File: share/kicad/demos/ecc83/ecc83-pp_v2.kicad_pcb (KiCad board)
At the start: 2 copper layers, 48.3 x 41.9 mm, 15 parts, among them P1 IN, P2 OUT, P3 POWER, P4 CONN_2, P5 CONN_1, P6 CONN_1, P7 CONN_1, P8 CONN_1, U1 ECC83

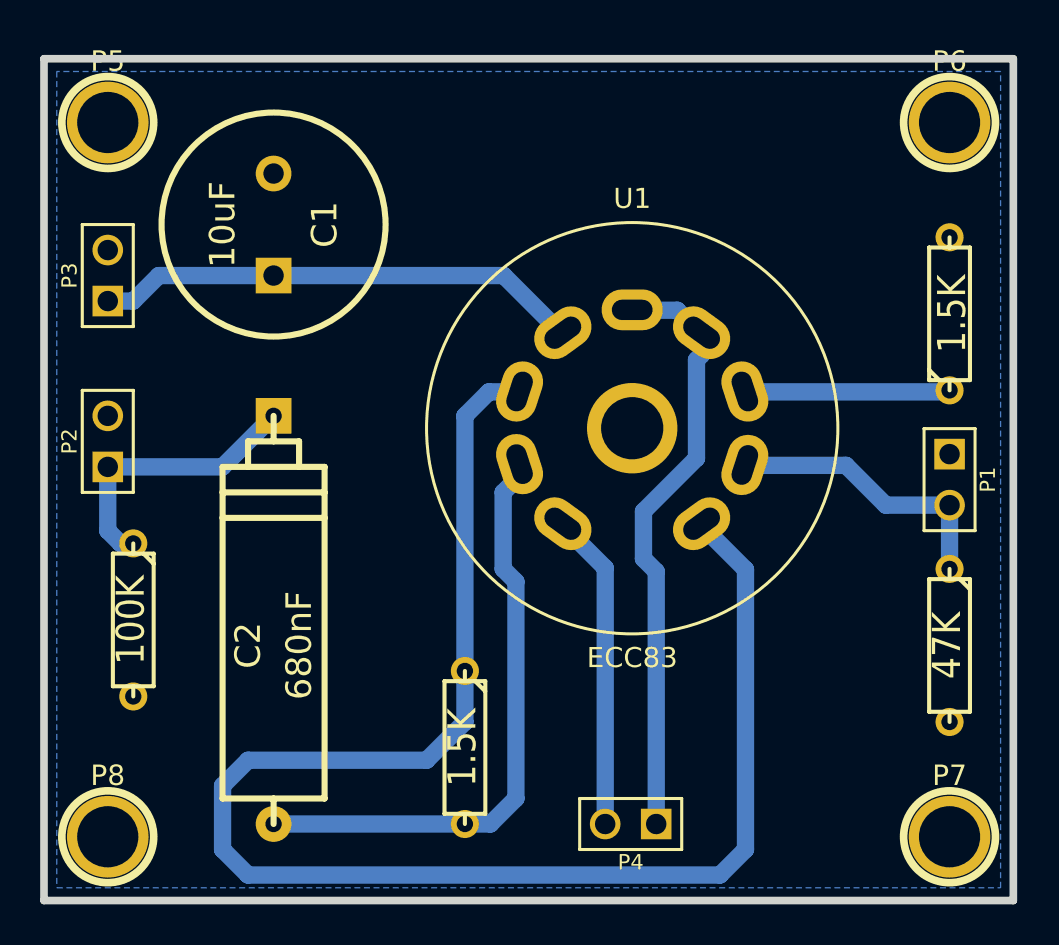
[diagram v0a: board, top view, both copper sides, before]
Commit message: Remove KiCad V4.0.7
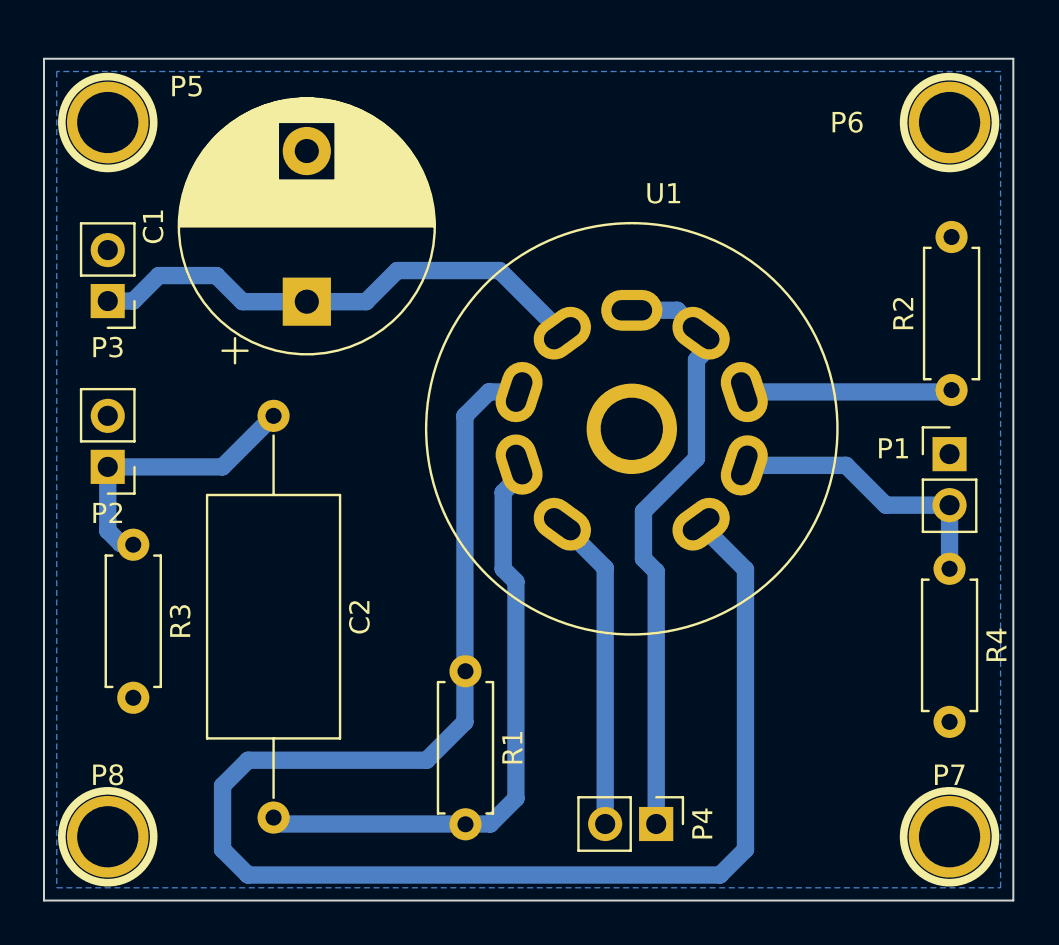
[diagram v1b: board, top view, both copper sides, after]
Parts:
- C1: footprint discret:C2V10 -> Capacitor_THT:CP_Radial_D12.5mm_P7.50mm
- C2: footprint discret:CP8 -> Capacitors_THT:C_Axial_L12.0mm_D6.5mm_P20.00mm_Horizontal
- P1, P2, P3, P4: footprint pin_array:pin_array_1x02 -> Connector_PinHeader_2.54mm:PinHeader_1x02_P2.54mm_Vertical
- R1, R2, R3, R4: footprint discret:R3 -> Resistor_THT:R_Axial_DIN0207_L6.3mm_D2.5mm_P7.62mm_Horizontal
- U1: footprint Valves:VALVE-ECC-83-2 -> Valve:Valve_ECC-83-2
- moved C2 10.2 mm to (131.4, 108.6)
- moved C1 4.18 mm to (133.1, 102.9)
- moved R4 3.81 mm to (165.1, 116.2)
- moved R2 3.80 mm to (165.2, 107.3)
- moved R1 3.80 mm to (141.0, 121.3)
- moved R3 3.75 mm to (124.5, 115.0)
- moved P1 1.27 mm to (165.1, 110.5), turned to 0 degrees
- moved P3 1.27 mm to (123.2, 102.9), turned to 180 degrees
- moved P4 1.27 mm to (150.5, 128.9), turned to -90 degrees
- moved P2 1.27 mm to (123.2, 111.1), turned to 180 degrees
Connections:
- P5 pad 1: Net-(P5-Pad1) -> unconnected-(P5-Pad1)
- P6 pad 1: Net-(P6-Pad1) -> unconnected-(P6-Pad1)
- P7 pad 1: Net-(P7-Pad1) -> unconnected-(P7-Pad1)
- P8 pad 1: Net-(P8-Pad1) -> unconnected-(P8-Pad1)
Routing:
- net Net-(C1-Pad1): track 24.3 -> 25.6 mm
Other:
- net class Default removed
- rule pad_to_mask_clearance: 0.1 -> 0
